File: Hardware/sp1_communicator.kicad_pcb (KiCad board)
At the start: 2 copper layers, 15 parts, among them J1 615006138421, J2 629722000214, U3 ESP32-C3-WROOM-02U-N4

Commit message: Schematic completed, started placing
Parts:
- added C4: 10uF, Capacitor_SMD:CP_Elec_6.3x5.7, F.Cu at (118.1, 84.5)
- added C5: 10uF, Capacitor_SMD:CP_Elec_6.3x5.7, F.Cu at (132.0, 84.5)
- added C6: 22uF, Capacitor_SMD:C_1210_3225Metric, F.Cu at (143.3, 86.3)
- added C7: 22uF, Capacitor_SMD:C_1210_3225Metric, F.Cu at (143.3, 89.7)
- added D2: 1N5819W, Diode_SMD:D_SOD-123, F.Cu at (107.9, 75.3)
- added D3: 1N5819W, Diode_SMD:D_SOD-123, F.Cu at (171.3, 86.5)
- added L1: 1uH, Inductor_SMD:L_Wuerth_WE-PD2-Typ-MS, F.Cu at (125.0, 87.2)
- added U1: 140357145100, Package_SO:SOP-4_3.8x4.1mm_P2.54mm, F.Cu at (115.3, 76.7)
- added U2: 140357145100, Package_SO:SOP-4_3.8x4.1mm_P2.54mm, F.Cu at (115.4, 68.3)
- added U4: ESP32-C3-WROOM-02U-N4, manul_tech:MODULE_ESP32-C3-WROOM-02-H4, F.Cu at (134.5, 63.2)
- U3: value ESP32-C3-WROOM-02U-N4 -> 173950336; footprint manul_tech:XCVR_ESP32-C3-WROOM-02U-N4 -> manul_tech:SIP3_11.6x8.5mm
- moved U3 33.4 mm to (139.3, 82.2)
- moved J2 4.15 mm to (186.9, 77.3)
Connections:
- R4 pad 1: /Interface/RQ -> /CPU/RQ
- R5 pad 2: /Interface/DATA -> /CPU/DATA
- U3 pad 1: +3V3 -> Net-(U3-VIN)
- U3 pad 2: /CPU/EN -> GND
- U3 pad 3: unconnected-(U3-IO4-Pad3) -> +3V3

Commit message: Completed routing
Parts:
- added C8: 100nF, Capacitor_SMD:C_0402_1005Metric, F.Cu at (105.4, 90.9)
- added C9: 100nF, Capacitor_SMD:C_0402_1005Metric, F.Cu at (98.8, 90.9)
- added R10: 220R, Resistor_SMD:R_0402_1005Metric, F.Cu at (101.9, 90.8)
- added R11: 220R, Resistor_SMD:R_0402_1005Metric, F.Cu at (95.3, 90.8)
- added R9: 10K, Resistor_SMD:R_0402_1005Metric, F.Cu at (107.8, 94.2)
- added SW1: KSEM31JLFS, manul_tech:KSEM31JLFS, F.Cu at (97.3, 96.7)
- added SW2: KSEM31JLFS, manul_tech:KSEM31JLFS, F.Cu at (103.9, 96.6)
- moved D3 63.1 mm to (108.3, 88.7), turned to -90 degrees
- moved R3 55.5 mm to (110.6, 67.1)
- moved R6 54.7 mm to (136.6, 91.2), turned to -90 degrees
- moved R1 54.0 mm to (110.6, 78.0)
- moved J2 53.2 mm to (137.9, 98.0), turned to 0 degrees
- moved R8 52.2 mm to (121.6, 72.1)
- moved R2 51.7 mm to (113.1, 73.8)
- moved R7 51.3 mm to (139.6, 91.2), turned to 90 degrees
- moved C2 50.7 mm to (121.1, 70.1), turned to 90 degrees
- moved C1 50.3 mm to (122.2, 70.1), turned to 90 degrees
- moved C3 48.7 mm to (123.3, 72.5), turned to -90 degrees
- moved R5 48.1 mm to (118.2, 71.2), turned to 180 degrees
- moved R4 44.2 mm to (120.7, 76.6), turned to -90 degrees
- moved D1 37.7 mm to (137.9, 86.4), turned to 90 degrees
- moved U3 29.2 mm to (115.3, 98.8)
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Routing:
- net VBUS: track 0.00 -> 48.1 mm, vias 0 -> 4
- net /CPU/EN: track 0.00 -> 37.7 mm, vias 0 -> 2
- net /CPU/BOOT: track 0.00 -> 28.4 mm, vias 0 -> 2
- net +5V: track 0.00 -> 22.4 mm, vias 0 -> 1
- net /CPU/DATA: track 0.00 -> 22.1 mm
- net /Interface/REQ: track 0.00 -> 13.1 mm
- net /CPU/DA+: track 0.00 -> 12.6 mm
- net /CPU/DA-: track 0.00 -> 11.9 mm
- net +3V3: track 0.00 -> 9.53 mm, vias 0 -> 6
- net /Interface/~{DATA}: track 0.00 -> 8.51 mm
- net /CPU/D+: track 0.00 -> 7.42 mm, vias 0 -> 1
- net /CPU/D-: track 0.00 -> 7.41 mm, vias 0 -> 1
- net Net-(D2-K): track 0.00 -> 5.45 mm
- net /CPU/RQ: track 0.00 -> 4.61 mm
- net Net-(R4-Pad2): track 0.00 -> 3.02 mm
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- added copper zone on F.Cu, net +3V3
- added copper zone on In1.Cu, net +3V3
- added copper zone on B.Cu, net GND
- added copper zone on F.Cu, net GND
- added copper zone on In2.Cu, net GND
- added copper zone on F.Cu, net Net-(D2-K)
- added copper zone on F.Cu, net Net-(U3-VIN)
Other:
- board outline added: 50.7 x 40 mm
- copper layers 2 -> 4
- board text added: "BOOT"
- board text added: "RESET"

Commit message: completed routing
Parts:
- added C10: TBD, Capacitor_SMD:C_0402_1005Metric, F.Cu at (136.4, 86.3)
- added C11: TBD, Capacitor_SMD:C_0402_1005Metric, F.Cu at (139.3, 86.3)
- added R12: 10K, Resistor_SMD:R_0402_1005Metric, F.Cu at (123.3, 70.1)
- added R13: 0R, Resistor_SMD:R_0402_1005Metric, F.Cu at (136.9, 84.8)
- added R14: 0R, Resistor_SMD:R_0402_1005Metric, F.Cu at (138.8, 84.8)
- C1: value 100nF -> 10uF
- C2: value 10uF -> 100nF
- R4: value 220R -> 10K
- R5: value 10K -> 220R
- moved R10 6.60 mm to (95.3, 90.8)
- moved R11 6.60 mm to (101.9, 90.8)
- moved R4 5.96 mm to (118.2, 71.2), turned to 180 degrees
- moved R5 5.96 mm to (120.7, 76.6), turned to -90 degrees
- moved C1 2.70 mm to (123.3, 72.5), turned to -90 degrees
- moved C3 2.70 mm to (122.2, 70.1), turned to 90 degrees
- moved D1 2.63 mm to (137.9, 89.1)
- moved R6 1.41 mm to (135.6, 90.2)
- moved J2 1.31 mm to (137.9, 99.4)
- moved R7 1.11 mm to (140.1, 90.2)
- moved SW1 0.05 mm to (97.3, 96.6)
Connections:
- net /CPU/BOOT renamed /BOOT
- net /CPU/D+ renamed /D+
- net /CPU/D- renamed /D-
- net /Interface/REQ renamed /REQ
- net /Interface/~{DATA} renamed /~{DATA}
- C1 pad 1: +3V3 -> /EN
- C3 pad 1: /CPU/EN -> +3V3
- C9 pad 2: /CPU/EN -> /EN
- D1 pad 4: /CPU/DA- -> Net-(C11-Pad1)
- D1 pad 6: /CPU/DA+ -> Net-(C10-Pad1)
- R4 pad 1: /CPU/RQ -> +3V3
- R4 pad 2: Net-(R4-Pad2) -> /RX
- R5 pad 1: +3V3 -> /RTS
- R5 pad 2: /CPU/DATA -> Net-(R5-Pad2)
- R8 pad 2: /CPU/EN -> /EN
- SW1 pad 1: /CPU/EN -> /EN
- SW1 pad 3: Net-(R11-Pad1) -> Net-(R10-Pad1)
- SW2 pad 3: Net-(R10-Pad1) -> Net-(R11-Pad1)
- U1 pad 1: Net-(R4-Pad2) -> Net-(R5-Pad2)
- U2 pad 4: /CPU/DATA -> /RX
- U4 pad 13: /CPU/DA- -> /DA-
- U4 pad 14: /CPU/DA+ -> /DA+
- U4 pad 16: unconnected-(U4-IO2-Pad16) -> Net-(U4-IO2)
- U4 pad 2: /CPU/EN -> /EN
- U4 pad 4: /CPU/RQ -> /RTS
- U4 pad 5: /CPU/DATA -> /RX
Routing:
- net /EN: track 0.00 -> 37.7 mm, vias 0 -> 2
- net /CPU/EN: track 37.7 -> 0.00 mm, vias 2 -> 0
- net Net-(U4-IO2): track 0.00 -> 23.9 mm, vias 0 -> 2
- net /RX: track 0.00 -> 22.1 mm, vias 0 -> 2
- net /CPU/DATA: track 22.1 -> 0.00 mm
- net /CPU/DA+: track 12.6 -> 0.00 mm
- net /CPU/DA-: track 11.9 -> 0.00 mm
- net /DA+: track 0.00 -> 11.5 mm
- net /DA-: track 0.00 -> 10.8 mm
- net /RTS: track 0.00 -> 4.61 mm
- net /CPU/RQ: track 4.61 -> 0.00 mm
- net /D-: track 7.41 -> 10.6 mm, vias 1 -> 2
- net Net-(R5-Pad2): track 0.00 -> 3.02 mm
- net Net-(R4-Pad2): track 3.02 -> 0.00 mm
- net Net-(J2-CC1): track 1.55 -> 4.27 mm
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
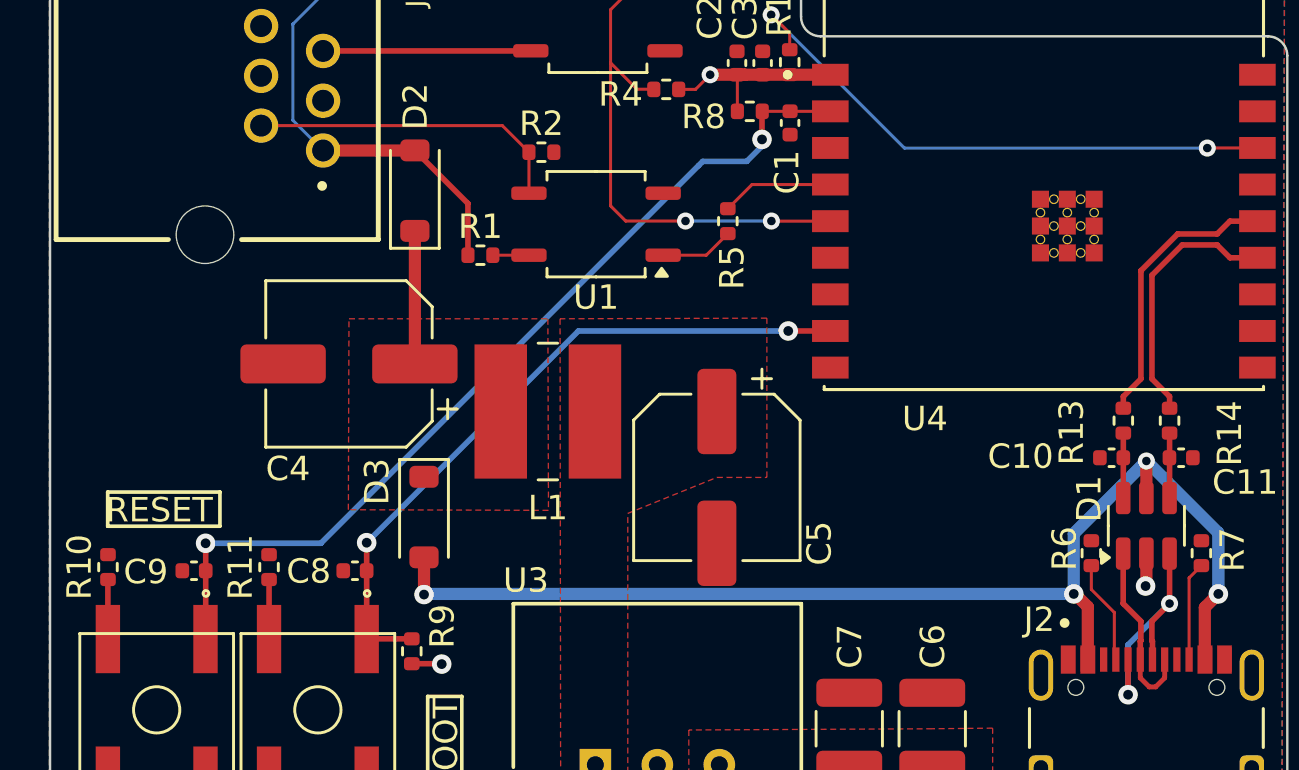
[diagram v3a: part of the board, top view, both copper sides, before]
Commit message: Added status led and power led and mounting holes
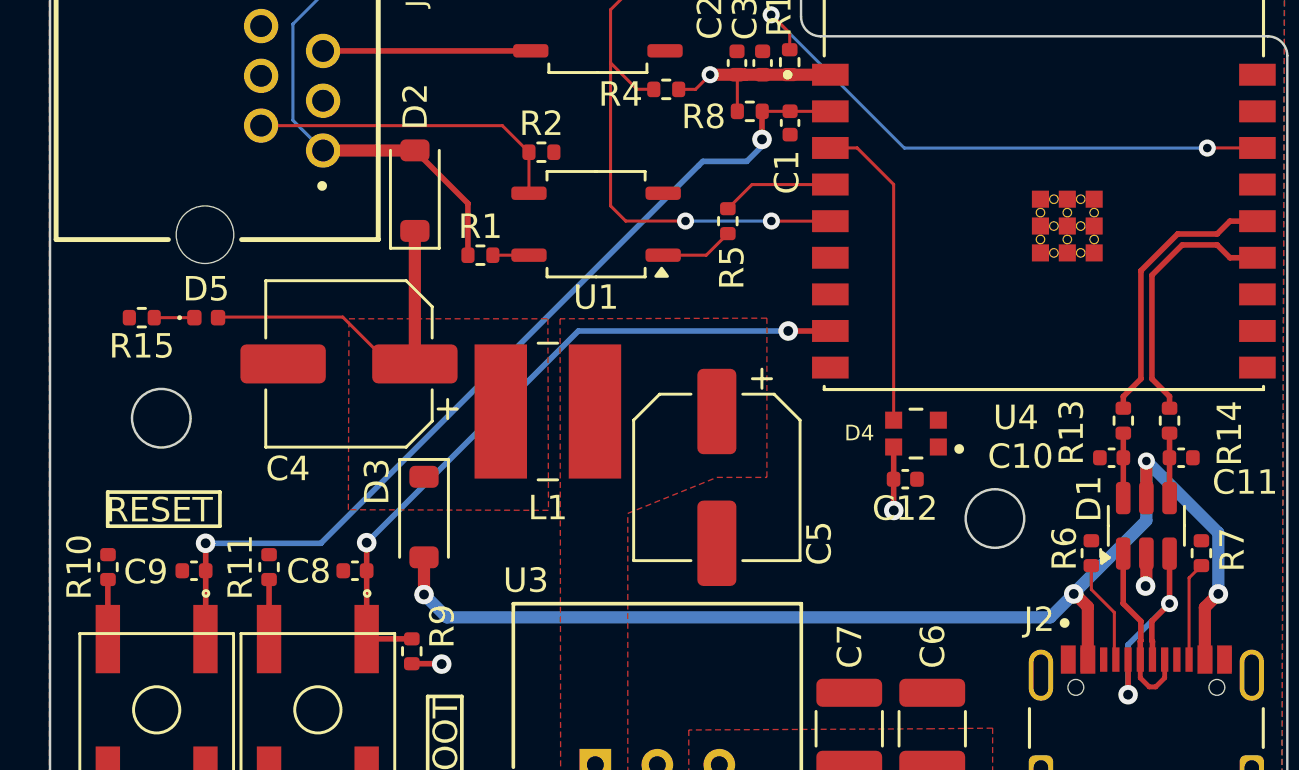
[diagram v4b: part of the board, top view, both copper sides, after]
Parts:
- added C12: 100nF, Capacitor_SMD:C_0402_1005Metric, F.Cu at (128.0, 87.2)
- added D4: WS2812C-2020, manul_tech:LED_WS2812C-2020, F.Cu at (128.4, 85.3)
- added D5: PWR, LED_SMD:LED_0402_1005Metric, F.Cu at (99.3, 80.5)
- added R15: 220R, Resistor_SMD:R_0402_1005Metric, F.Cu at (96.7, 80.5)
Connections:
- U4 pad 19: (no net) -> GND
- U4 pad 20: (no net) -> GND
- U4 pad 21: (no net) -> GND
- U4 pad 22: (no net) -> GND
- U4 pad 23: (no net) -> GND
- U4 pad 24: (no net) -> GND
- U4 pad 25: (no net) -> GND
- U4 pad 26: (no net) -> GND
- U4 pad 27: (no net) -> GND
- U4 pad 28: (no net) -> GND
- U4 pad 29: (no net) -> GND
- U4 pad 3: unconnected-(U4-IO4-Pad3) -> /STATUS_LED
- U4 pad 30: (no net) -> GND
- U4 pad 31: (no net) -> GND
- U4 pad 32: (no net) -> GND
- U4 pad 33: (no net) -> GND
- U4 pad 34: (no net) -> GND
- U4 pad 35: (no net) -> GND
- U4 pad 36: (no net) -> GND
- U4 pad 37: (no net) -> GND
- U4 pad 38: (no net) -> GND
- U4 pad 39: (no net) -> GND
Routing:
- net /STATUS_LED: track 0.00 -> 12.9 mm
- net Net-(D2-K): track 5.45 -> 14.3 mm
- net +3V3: track 9.53 -> 12.1 mm, vias 6 -> 7
- net Net-(D5-K): track 0.00 -> 1.64 mm
- net VBUS: track 48.8 -> 49.6 mm
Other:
- outline, holes or cut-outs redrawn
- board text added: "P1 Wireless Interface (P1WI) designed by Manul Technologies 2024 V1.0"
